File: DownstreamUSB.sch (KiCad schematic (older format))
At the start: 5 parts, among them J4 USB_A

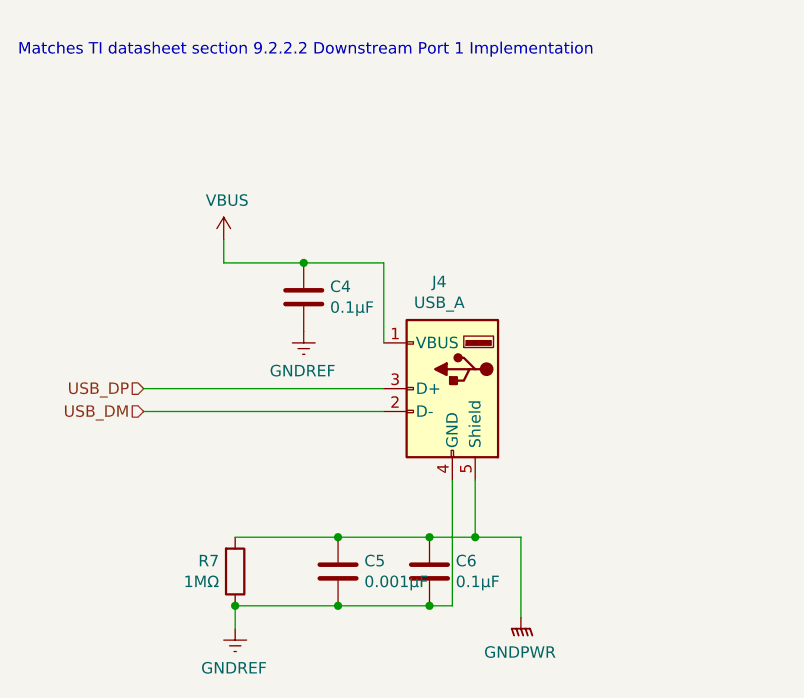
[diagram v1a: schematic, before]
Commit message: First pass at audio
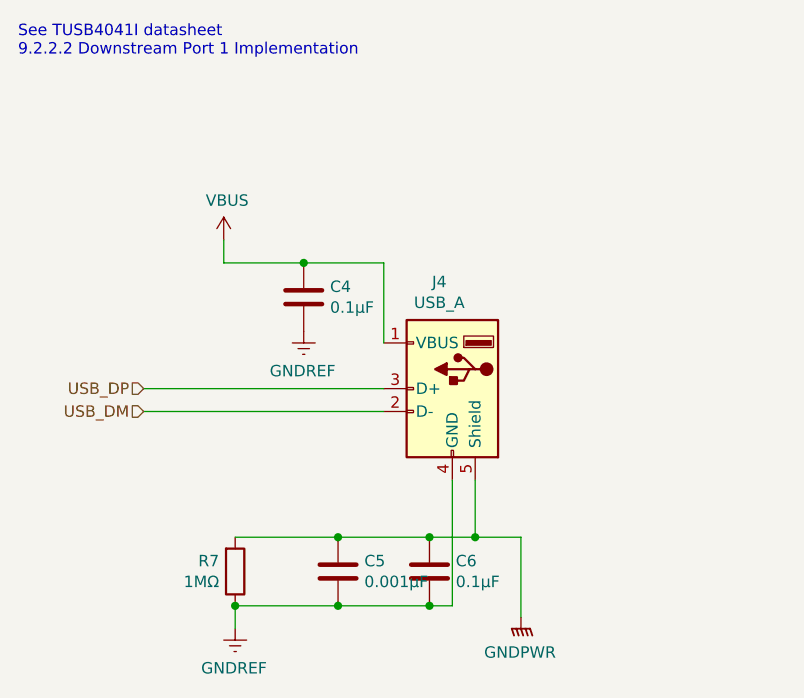
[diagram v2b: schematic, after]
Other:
- note added: "See TUSB4041I datasheet\n9.2.2.2 Downstream Port 1 Implementation"
- note removed: "Matches TI datasheet section 9.2.2.2 Downstream Port 1 Implementation"
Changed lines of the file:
@@
 Connection ~ 5250 2850
 Text Notes 4000 1950 0    50   ~ 0
-Matches TI datasheet section 9.2.2.2 Downstream Port 1 Implementation
+See TUSB4041I datasheet\n9.2.2.2 Downstream Port 1 Implementation
 $EndSCHEMATC

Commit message: First pass at pcb layout
Not really ready to set that in stone, but wanted to get an idea of what size enclosure will work.
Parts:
- C4, C5, C6: footprint (none) -> Capacitor_SMD:C_1210_3225Metric
- J4: footprint (none) -> Connector_USB:USB_A_Molex_67643_Horizontal
- R7: footprint (none) -> Resistor_SMD:R_1210_3225Metric
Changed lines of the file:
@@
 $Descr A4 11693 8268
 encoding utf-8
-Sheet 5 6
+Sheet 4 6
 Title ""
 Date ""
@@
 F 0 "J4" H 5957 3867 50  0000 C CNN
 F 1 "USB_A" H 5957 3776 50  0000 C CNN
-F 2 "" H 6050 3350 50  0001 C CNN
+F 2 "Connector_USB:USB_A_Molex_67643_Horizontal" H 6050 3350 50  0001 C CNN
 F 3 " ~" H 6050 3350 50  0001 C CNN
 	1    5900 3400
@@
 $EndComp
 $Comp
-L power:VBUS #PWR?
+L power:VBUS #PWR0113
 U 1 1 605E55CB
 P 4900 2750
-F 0 "#PWR?" H 4900 2600 50  0001 C CNN
+F 0 "#PWR0113" H 4900 2600 50  0001 C CNN
 F 1 "VBUS" H 4915 2923 50  0000 C CNN
 F 2 "" H 4900 2750 50  0001 C CNN
@@
 F 0 "R7" H 4880 4154 50  0000 R CNN
 F 1 "1MΩ" H 4880 4245 50  0000 R CNN
-F 2 "" V 4880 4200 50  0001 C CNN
+F 2 "Resistor_SMD:R_1210_3225Metric" V 4880 4200 50  0001 C CNN
 F 3 "~" H 4950 4200 50  0001 C CNN
 	1    4950 4200
@@
 F 0 "C5" H 5285 4246 50  0000 R CNN
 F 1 "0.001μF" H 5285 4155 50  0000 R CNN
-F 2 "" H 5438 4050 50  0001 C CNN
+F 2 "Capacitor_SMD:C_1210_3225Metric" H 5438 4050 50  0001 C CNN
 F 3 "~" H 5400 4200 50  0001 C CNN
 	1    5400 4200
@@
 F 0 "C6" H 5685 4246 50  0000 R CNN
 F 1 "0.1μF" H 5685 4155 50  0000 R CNN
-F 2 "" H 5838 4050 50  0001 C CNN
+F 2 "Capacitor_SMD:C_1210_3225Metric" H 5838 4050 50  0001 C CNN
 F 3 "~" H 5800 4200 50  0001 C CNN
 	1    5800 4200
@@
 P 6200 4400
 AR Path="/6057976E/605E91F3" Ref="#PWR?"  Part="1"
-AR Path="/605B3ED2/605E91F3" Ref="#PWR?"  Part="1"
-F 0 "#PWR?" H 6200 4200 50  0001 C CNN
+AR Path="/605B3ED2/605E91F3" Ref="#PWR0114"  Part="1"
+F 0 "#PWR0114" H 6200 4200 50  0001 C CNN
 F 1 "GNDPWR" H 6204 4246 50  0000 C CNN
 F 2 "" H 6200 4350 50  0001 C CNN
@@
 P 4950 4450
 AR Path="/6057976E/605E91FC" Ref="#PWR?"  Part="1"
-AR Path="/605B3ED2/605E91FC" Ref="#PWR?"  Part="1"
-F 0 "#PWR?" H 4950 4200 50  0001 C CNN
+AR Path="/605B3ED2/605E91FC" Ref="#PWR0115"  Part="1"
+F 0 "#PWR0115" H 4950 4200 50  0001 C CNN
 F 1 "GNDREF" H 4955 4277 50  0000 C CNN
 F 2 "" H 4950 4450 50  0001 C CNN
@@
 F 0 "C4" H 5135 3046 50  0000 R CNN
 F 1 "0.1μF" H 5135 2955 50  0000 R CNN
-F 2 "" H 5288 2850 50  0001 C CNN
+F 2 "Capacitor_SMD:C_1210_3225Metric" H 5288 2850 50  0001 C CNN
 F 3 "~" H 5250 3000 50  0001 C CNN
 	1    5250 3000
@@
 P 5250 3150
 AR Path="/6057976E/605EED26" Ref="#PWR?"  Part="1"
-AR Path="/605B3ED2/605EED26" Ref="#PWR?"  Part="1"
-F 0 "#PWR?" H 5250 2900 50  0001 C CNN
+AR Path="/605B3ED2/605EED26" Ref="#PWR0116"  Part="1"
+F 0 "#PWR0116" H 5250 2900 50  0001 C CNN
 F 1 "GNDREF" H 5255 2977 50  0000 C CNN
 F 2 "" H 5250 3150 50  0001 C CNN

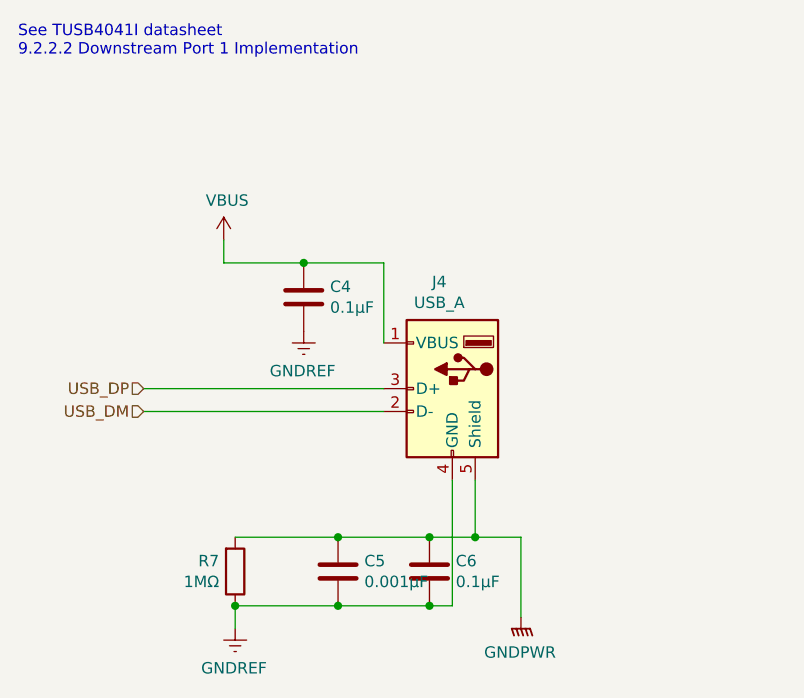
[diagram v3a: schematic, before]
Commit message: Swap TUSB4041I for TUSB2036
The 4041 does more than I need it to, so use the 2036 instead.
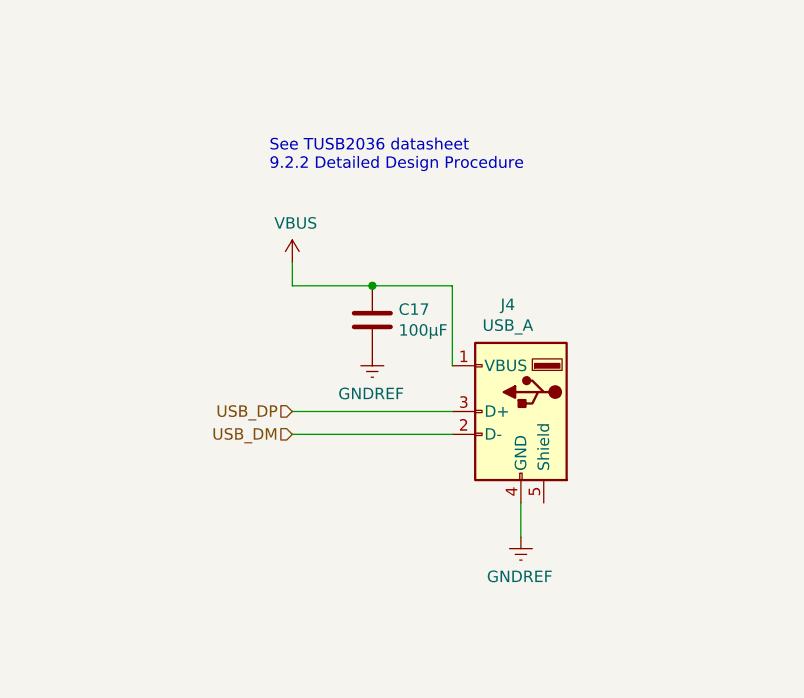
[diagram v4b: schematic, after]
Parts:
- removed C5: 0.001μF, Capacitor_SMD:C_1210_3225Metric, symbol Device:C
- removed C6: 0.1μF, Capacitor_SMD:C_1210_3225Metric, symbol Device:C
- removed R7: 1MΩ, Resistor_SMD:R_1210_3225Metric, symbol Device:R
- C17: renamed from C4; value 0.1μF -> 100μF; footprint Capacitor_SMD:C_1210_3225Metric -> Capacitor_SMD:CP_Elec_4x3
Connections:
- net GNDPWR: no longer names the net of J4.5 (Shield)
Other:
- note added: "See TUSB2036 datasheet\n9.2.2 Detailed Design Procedure"
- note removed: "See TUSB4041I datasheet\n9.2.2.2 Downstream Port 1 Implementation"
- moved on the sheet: C17, J4
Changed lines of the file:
@@
 $Descr A4 11693 8268
 encoding utf-8
-Sheet 4 6
+Sheet 6 6
 Title ""
 Date ""
@@
 Comment4 ""
 $EndDescr
+Text Notes 5100 2450 0    50   ~ 0
+See TUSB2036 datasheet\n9.2.2 Detailed Design Procedure
+$Comp
+L power:GNDREF #PWR?
+U 1 1 6054D05F
+P 5550 3250
+AR Path="/6057976E/6054D05F" Ref="#PWR?"  Part="1"
+AR Path="/605B3ED2/6054D05F" Ref="#PWR0134"  Part="1"
+F 0 "#PWR0134" H 5550 3000 50  0001 C CNN
+F 1 "GNDREF" H 5555 3077 50  0000 C CNN
+F 2 "" H 5550 3250 50  0001 C CNN
+F 3 "" H 5550 3250 50  0001 C CNN
+	1    5550 3250
+	-1   0    0    -1
+$EndComp
+Wire Wire Line
+	6200 4050 6200 3900
+Wire Wire Line
+	5900 2950 5900 3300
+Wire Wire Line
+	5200 2850 5200 2950
+$Comp
+L power:GNDREF #PWR?
+U 1 1 605EED26
+P 6200 4050
+AR Path="/6057976E/605EED26" Ref="#PWR?"  Part="1"
+AR Path="/605B3ED2/605EED26" Ref="#PWR0116"  Part="1"
+F 0 "#PWR0116" H 6200 3800 50  0001 C CNN
+F 1 "GNDREF" H 6205 3877 50  0000 C CNN
+F 2 "" H 6200 4050 50  0001 C CNN
+F 3 "" H 6200 4050 50  0001 C CNN
+	1    6200 4050
+	-1   0    0    -1
+$EndComp
+Wire Wire Line
+	5550 2950 5900 2950
+Wire Wire Line
+	5200 2950 5550 2950
+Connection ~ 5550 2950
+$Comp
+L power:VBUS #PWR0113
+U 1 1 605E55CB
+P 5200 2850
+F 0 "#PWR0113" H 5200 2700 50  0001 C CNN
+F 1 "VBUS" H 5215 3023 50  0000 C CNN
+F 2 "" H 5200 2850 50  0001 C CNN
+F 3 "" H 5200 2850 50  0001 C CNN
+	1    5200 2850
+	1    0    0    -1
+$EndComp
 $Comp
 L Connector:USB_A J?
 U 1 1 605B68EE
-P 5900 3400
+P 6200 3500
 AR Path="/605B68EE" Ref="J?"  Part="1"
 AR Path="/605B3ED2/605B68EE" Ref="J4"  Part="1"
-F 0 "J4" H 5957 3867 50  0000 C CNN
-F 1 "USB_A" H 5957 3776 50  0000 C CNN
-F 2 "Connector_USB:USB_A_Molex_67643_Horizontal" H 6050 3350 50  0001 C CNN
-F 3 " ~" H 6050 3350 50  0001 C CNN
-	1    5900 3400
-	-1   0    0    -1
-$EndComp
-$Comp
-L power:VBUS #PWR0113
-U 1 1 605E55CB
-P 4900 2750
-F 0 "#PWR0113" H 4900 2600 50  0001 C CNN
-F 1 "VBUS" H 4915 2923 50  0000 C CNN
-F 2 "" H 4900 2750 50  0001 C CNN
-F 3 "" H 4900 2750 50  0001 C CNN
-	1    4900 2750
-	1    0    0    -1
-$EndComp
-Text HLabel 4550 3400 0    50   Input ~ 0
-USB_DP
-Text HLabel 4550 3500 0    50   Input ~ 0
-USB_DM
-Wire Wire Line
-	4550 3400 5600 3400
-Wire Wire Line
-	4550 3500 5600 3500
-Connection ~ 4950 4350
-Wire Wire Line
-	4950 4350 4950 4450
-Connection ~ 5400 4350
-Wire Wire Line
-	5400 4350 4950 4350
-Connection ~ 5800 4350
-Wire Wire Line
-	5800 4350 5400 4350
-Wire Wire Line
-	5900 4350 5800 4350
-Wire Wire Line
-	5900 3800 5900 4350
-Connection ~ 5400 4050
-Wire Wire Line
-	5400 4050 4950 4050
-Connection ~ 5800 4050
-Wire Wire Line
-	5400 4050 5800 4050
-Wire Wire Line
-	6000 4050 5800 4050
-Wire Wire Line
-	6000 3800 6000 4050
-$Comp
-L Device:R R?
-U 1 1 605E91E1
-P 4950 4200
-AR Path="/605E91E1" Ref="R?"  Part="1"
-AR Path="/6057976E/605E91E1" Ref="R?"  Part="1"
-AR Path="/605B3ED2/605E91E1" Ref="R7"  Part="1"
-F 0 "R7" H 4880 4154 50  0000 R CNN
-F 1 "1MΩ" H 4880 4245 50  0000 R CNN
-F 2 "Resistor_SMD:R_1210_3225Metric" V 4880 4200 50  0001 C CNN
-F 3 "~" H 4950 4200 50  0001 C CNN
-	1    4950 4200
-	1    0    0    1
-$EndComp
-$Comp
-L Device:C C?
-U 1 1 605E91E7
-P 5400 4200
-AR Path="/605E91E7" Ref="C?"  Part="1"
-AR Path="/6057976E/605E91E7" Ref="C?"  Part="1"
-AR Path="/605B3ED2/605E91E7" Ref="C5"  Part="1"
-F 0 "C5" H 5285 4246 50  0000 R CNN
-F 1 "0.001μF" H 5285 4155 50  0000 R CNN
-F 2 "Capacitor_SMD:C_1210_3225Metric" H 5438 4050 50  0001 C CNN
-F 3 "~" H 5400 4200 50  0001 C CNN
-	1    5400 4200
-	-1   0    0    -1
-$EndComp
-$Comp
-L Device:C C?
-U 1 1 605E91ED
-P 5800 4200
-AR Path="/605E91ED" Ref="C?"  Part="1"
-AR Path="/6057976E/605E91ED" Ref="C?"  Part="1"
-AR Path="/605B3ED2/605E91ED" Ref="C6"  Part="1"
-F 0 "C6" H 5685 4246 50  0000 R CNN
-F 1 "0.1μF" H 5685 4155 50  0000 R CNN
-F 2 "Capacitor_SMD:C_1210_3225Metric" H 5838 4050 50  0001 C CNN
-F 3 "~" H 5800 4200 50  0001 C CNN
-	1    5800 4200
-	-1   0    0    -1
-$EndComp
-$Comp
-L power:GNDPWR #PWR?
-U 1 1 605E91F3
-P 6200 4400
-AR Path="/6057976E/605E91F3" Ref="#PWR?"  Part="1"
-AR Path="/605B3ED2/605E91F3" Ref="#PWR0114"  Part="1"
-F 0 "#PWR0114" H 6200 4200 50  0001 C CNN
-F 1 "GNDPWR" H 6204 4246 50  0000 C CNN
-F 2 "" H 6200 4350 50  0001 C CNN
-F 3 "" H 6200 4350 50  0001 C CNN
-	1    6200 4400
-	-1   0    0    -1
-$EndComp
-Connection ~ 6000 4050
-Wire Wire Line
-	6000 4050 6200 4050
-Wire Wire Line
-	6200 4050 6200 4400
-$Comp
-L power:GNDREF #PWR?
-U 1 1 605E91FC
-P 4950 4450
-AR Path="/6057976E/605E91FC" Ref="#PWR?"  Part="1"
-AR Path="/605B3ED2/605E91FC" Ref="#PWR0115"  Part="1"
-F 0 "#PWR0115" H 4950 4200 50  0001 C CNN
-F 1 "GNDREF" H 4955 4277 50  0000 C CNN
-F 2 "" H 4950 4450 50  0001 C CNN
-F 3 "" H 4950 4450 50  0001 C CNN
-	1    4950 4450
+F 0 "J4" H 6257 3967 50  0000 C CNN
+F 1 "USB_A" H 6257 3876 50  0000 C CNN
+F 2 "Connector_USB:USB_A_Molex_67643_Horizontal" H 6350 3450 50  0001 C CNN
+F 3 " ~" H 6350 3450 50  0001 C CNN
+	1    6200 3500
 	-1   0    0    -1
 $EndComp
@@
 L Device:C C?
 U 1 1 605EE4F2
-P 5250 3000
+P 5550 3100
 AR Path="/605EE4F2" Ref="C?"  Part="1"
 AR Path="/6057976E/605EE4F2" Ref="C?"  Part="1"
-AR Path="/605B3ED2/605EE4F2" Ref="C4"  Part="1"
-F 0 "C4" H 5135 3046 50  0000 R CNN
-F 1 "0.1μF" H 5135 2955 50  0000 R CNN
-F 2 "Capacitor_SMD:C_1210_3225Metric" H 5288 2850 50  0001 C CNN
-F 3 "~" H 5250 3000 50  0001 C CNN
-	1    5250 3000
+AR Path="/605B3ED2/605EE4F2" Ref="C17"  Part="1"
+F 0 "C17" H 5435 3146 50  0000 R CNN
+F 1 "100μF" H 5435 3055 50  0000 R CNN
+F 2 "Capacitor_SMD:CP_Elec_4x3" H 5588 2950 50  0001 C CNN
+F 3 "~" H 5550 3100 50  0001 C CNN
+	1    5550 3100
 	-1   0    0    -1
 $EndComp
-$Comp
-L power:GNDREF #PWR?
-U 1 1 605EED26
-P 5250 3150
-AR Path="/6057976E/605EED26" Ref="#PWR?"  Part="1"
-AR Path="/605B3ED2/605EED26" Ref="#PWR0116"  Part="1"
-F 0 "#PWR0116" H 5250 2900 50  0001 C CNN
-F 1 "GNDREF" H 5255 2977 50  0000 C CNN
-F 2 "" H 5250 3150 50  0001 C CNN
-F 3 "" H 5250 3150 50  0001 C CNN
-	1    5250 3150
-	-1   0    0    -1
-$EndComp
+Text HLabel 5200 3500 0    50   Input ~ 0
+USB_DP
+Text HLabel 5200 3600 0    50   Input ~ 0
+USB_DM
 Wire Wire Line
-	4900 2750 4900 2850
+	5200 3500 5900 3500
 Wire Wire Line
-	4900 2850 5250 2850
-Wire Wire Line
-	5250 2850 5600 2850
-Wire Wire Line
-	5600 2850 5600 3200
-Connection ~ 5250 2850
-Text Notes 4000 1950 0    50   ~ 0
-See TUSB4041I datasheet\n9.2.2.2 Downstream Port 1 Implementation
+	5200 3600 5900 3600
 $EndSCHEMATC

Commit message: Add BOM and clarify some footprints
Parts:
- C17: footprint Capacitor_SMD:CP_Elec_4x3 -> Capacitor_SMD:C_1210_3225Metric; Manufacturer_Name (none) -> AVX; Manufacturer_Part_Number (none) -> TPST107M004R0500; Price (none) -> 0.93; Vendor (none) -> Mouser; Vendor Part Number (none) -> 581-TPST107M004R0500
- J4: Description (none) -> Downstream USB socket; Manufacturer_Name (none) -> Molex; Manufacturer_Part_Number (none) -> 67643-3910; Price (none) -> 1.64; Vendor (none) -> Mouser; Vendor Part Number (none) -> 538-67643-3910
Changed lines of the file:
@@
 Comment4 ""
 $EndDescr
-Text Notes 5100 2450 0    50   ~ 0
-See TUSB2036 datasheet\n9.2.2 Detailed Design Procedure
 $Comp
 L power:GNDREF #PWR?
@@
 	-1   0    0    -1
 $EndComp
-Wire Wire Line
-	6200 4050 6200 3900
-Wire Wire Line
-	5900 2950 5900 3300
-Wire Wire Line
-	5200 2850 5200 2950
 $Comp
 L power:GNDREF #PWR?
@@
 	-1   0    0    -1
 $EndComp
-Wire Wire Line
-	5550 2950 5900 2950
-Wire Wire Line
-	5200 2950 5550 2950
-Connection ~ 5550 2950
 $Comp
 L power:VBUS #PWR0113
@@
 F 1 "USB_A" H 6257 3876 50  0000 C CNN
 F 2 "Connector_USB:USB_A_Molex_67643_Horizontal" H 6350 3450 50  0001 C CNN
-F 3 " ~" H 6350 3450 50  0001 C CNN
+F 3 "https://www.mouser.com/datasheet/2/276/1/0676433910_IO_CONNECTORS-172273.pdf" H 6350 3450 50  0001 C CNN
+F 4 "Downstream USB socket" H 6257 4067 50  0001 C CNN "Description"
+F 5 "Molex" H 6257 4067 50  0001 C CNN "Manufacturer_Name"
+F 6 "67643-3910" H 6257 4067 50  0001 C CNN "Manufacturer_Part_Number"
+F 7 "1.64" H 6257 4067 50  0001 C CNN "Price"
+F 8 "538-67643-3910" H 6257 4067 50  0001 C CNN "Vendor Part Number"
+F 9 "Mouser" H 6257 4067 50  0001 C CNN "Vendor"
 	1    6200 3500
 	-1   0    0    -1
@@
 F 0 "C17" H 5435 3146 50  0000 R CNN
 F 1 "100μF" H 5435 3055 50  0000 R CNN
-F 2 "Capacitor_SMD:CP_Elec_4x3" H 5588 2950 50  0001 C CNN
-F 3 "~" H 5550 3100 50  0001 C CNN
+F 2 "Capacitor_SMD:C_1210_3225Metric" H 5588 2950 50  0001 C CNN
+F 3 "https://www.mouser.com/datasheet/2/40/TPS-2066671.pdf" H 5550 3100 50  0001 C CNN
+F 4 "AVX" H 5435 3246 50  0001 C CNN "Manufacturer_Name"
+F 5 "TPST107M004R0500" H 5435 3246 50  0001 C CNN "Manufacturer_Part_Number"
+F 6 "0.93" H 5435 3246 50  0001 C CNN "Price"
+F 7 "581-TPST107M004R0500" H 5435 3246 50  0001 C CNN "Vendor Part Number"
+F 8 "Mouser" H 5435 3246 50  0001 C CNN "Vendor"
 	1    5550 3100
 	-1   0    0    -1
 $EndComp
+Text Notes 5100 2450 0    50   ~ 0
+See TUSB2036 datasheet\n9.2.2 Detailed Design Procedure
 Text HLabel 5200 3500 0    50   Input ~ 0
 USB_DP
@@
 USB_DM
 Wire Wire Line
+	6200 4050 6200 3900
+Wire Wire Line
+	5900 2950 5900 3300
+Wire Wire Line
+	5200 2850 5200 2950
+Wire Wire Line
+	5550 2950 5900 2950
+Wire Wire Line
+	5200 2950 5550 2950
+Wire Wire Line
 	5200 3500 5900 3500
 Wire Wire Line
 	5200 3600 5900 3600
+Connection ~ 5550 2950
 $EndSCHEMATC
